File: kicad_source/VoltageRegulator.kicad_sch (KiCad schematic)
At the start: 40 parts, among them J10 x, J11 PowerPole, J12 Conn_01x02, Q2 IPD90P03P4L- 04, U12 INA226, U13 IFX91041EFJ

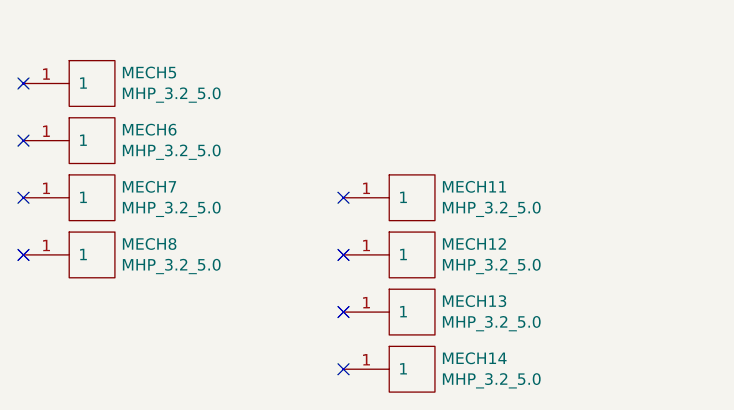
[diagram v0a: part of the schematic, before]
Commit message: added connector for quad encoder
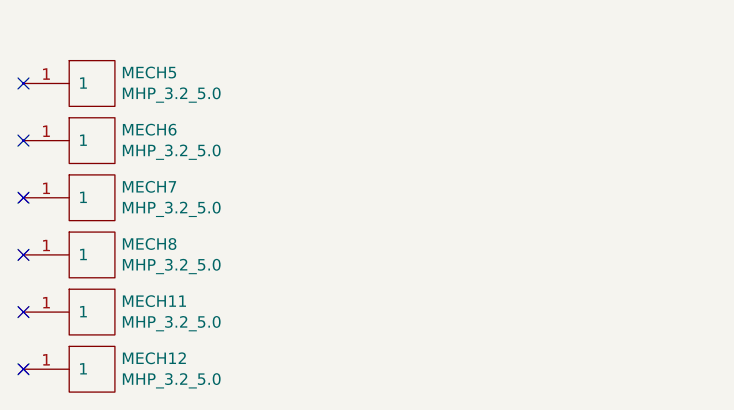
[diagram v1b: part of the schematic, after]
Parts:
- removed MECH13, MECH14: MHP_3.2_5.0, generationmake:MHP_3.2_5.8, symbol OpenCyphalRobotController07-rescue:MHP_3.2_5.0-MECH_mounting-holes
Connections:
- no-connect marks 9 -> 7
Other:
- moved on the sheet: MECH11, MECH12
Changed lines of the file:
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@@
   (junction (at 124.46 43.18) (diameter 0) (color 0 0 0 0)
   )
-  (no_connect (at 58.42 185.42))
   (no_connect (at 22.86 166.37))
   (no_connect (at 22.86 160.02))
   (no_connect (at 68.58 64.77))
   (no_connect (at 22.86 179.07))
-  (no_connect (at 58.42 172.72))
-  (no_connect (at 58.42 191.77))
-  (no_connect (at 58.42 179.07))
+  (no_connect (at 22.86 185.42))
+  (no_connect (at 22.86 191.77))
   (no_connect (at 22.86 172.72))
   (wire (pts (xy 189.23 128.27) (xy 189.23 127))
@@
     (pin "1")
   )
-  (symbol (lib_id "OpenCyphalRobotController07-rescue:MHP_3.2_5.0-MECH_mounting-holes") (at 66.04 172.72 0) (unit 1)
-    (in_bom yes) (on_board yes)
-    (property "Reference" "MECH11" (id 0) (at 69.2912 171.5516 0)
-      (effects (font (size 1.27 1.27)) (justify left))
-    )
-    (property "Value" "MHP_3.2_5.0" (id 1) (at 69.2912 173.863 0)
-      (effects (font (size 1.27 1.27)) (justify left))
-    )
-    (property "Footprint" "generationmake:MHP_3.2_5.8" (id 2) (at 63.5 171.45 0)
-      (effects (font (size 1.27 1.27)) hide)
-    )
-    (property "Datasheet" "" (id 3) (at 66.04 172.72 0)
-      (effects (font (size 1.27 1.27)) hide)
-    )
-    (pin "1")
-  )
-  (symbol (lib_id "OpenCyphalRobotController07-rescue:MHP_3.2_5.0-MECH_mounting-holes") (at 66.04 179.07 0) (unit 1)
-    (in_bom yes) (on_board yes)
-    (property "Reference" "MECH12" (id 0) (at 69.2912 177.9016 0)
-      (effects (font (size 1.27 1.27)) (justify left))
-    )
-    (property "Value" "MHP_3.2_5.0" (id 1) (at 69.2912 180.213 0)
-      (effects (font (size 1.27 1.27)) (justify left))
-    )
-    (property "Footprint" "generationmake:MHP_3.2_5.8" (id 2) (at 63.5 177.8 0)
-      (effects (font (size 1.27 1.27)) hide)
-    )
-    (property "Datasheet" "" (id 3) (at 66.04 179.07 0)
-      (effects (font (size 1.27 1.27)) hide)
-    )
-    (pin "1")
-  )
-  (symbol (lib_id "OpenCyphalRobotController07-rescue:MHP_3.2_5.0-MECH_mounting-holes") (at 66.04 185.42 0) (unit 1)
-    (in_bom yes) (on_board yes)
-    (property "Reference" "MECH13" (id 0) (at 69.2912 184.2516 0)
-      (effects (font (size 1.27 1.27)) (justify left))
-    )
-    (property "Value" "MHP_3.2_5.0" (id 1) (at 69.2912 186.563 0)
-      (effects (font (size 1.27 1.27)) (justify left))
-    )
-    (property "Footprint" "generationmake:MHP_3.2_5.8" (id 2) (at 63.5 184.15 0)
-      (effects (font (size 1.27 1.27)) hide)
-    )
-    (property "Datasheet" "" (id 3) (at 66.04 185.42 0)
-      (effects (font (size 1.27 1.27)) hide)
-    )
-    (pin "1")
-  )
-  (symbol (lib_id "OpenCyphalRobotController07-rescue:MHP_3.2_5.0-MECH_mounting-holes") (at 66.04 191.77 0) (unit 1)
-    (in_bom yes) (on_board yes)
-    (property "Reference" "MECH14" (id 0) (at 69.2912 190.6016 0)
-      (effects (font (size 1.27 1.27)) (justify left))
-    )
-    (property "Value" "MHP_3.2_5.0" (id 1) (at 69.2912 192.913 0)
-      (effects (font (size 1.27 1.27)) (justify left))
-    )
-    (property "Footprint" "generationmake:MHP_3.2_5.8" (id 2) (at 63.5 190.5 0)
-      (effects (font (size 1.27 1.27)) hide)
-    )
-    (property "Datasheet" "" (id 3) (at 66.04 191.77 0)
-      (effects (font (size 1.27 1.27)) hide)
-    )
+  (symbol (lib_id "OpenCyphalRobotController07-rescue:MHP_3.2_5.0-MECH_mounting-holes") (at 30.48 185.42 0) (unit 1)
+    (in_bom yes) (on_board yes)
+    (property "Reference" "MECH11" (id 0) (at 33.7312 184.2516 0)
+      (effects (font (size 1.27 1.27)) (justify left))
+    )
+    (property "Value" "MHP_3.2_5.0" (id 1) (at 33.7312 186.563 0)
+      (effects (font (size 1.27 1.27)) (justify left))
+    )
+    (property "Footprint" "generationmake:MHP_3.2_5.8" (id 2) (at 27.94 184.15 0)
+      (effects (font (size 1.27 1.27)) hide)
+    )
+    (property "Datasheet" "" (id 3) (at 30.48 185.42 0)
+      (effects (font (size 1.27 1.27)) hide)
+    )
+    (pin "1")
+  )
+  (symbol (lib_id "OpenCyphalRobotController07-rescue:MHP_3.2_5.0-MECH_mounting-holes") (at 30.48 191.77 0) (unit 1)
+    (in_bom yes) (on_board yes)
+    (property "Reference" "MECH12" (id 0) (at 33.7312 190.6016 0)
+      (effects (font (size 1.27 1.27)) (justify left))
+    )
+    (property "Value" "MHP_3.2_5.0" (id 1) (at 33.7312 192.913 0)
+      (effects (font (size 1.27 1.27)) (justify left))
+    )
+    (property "Footprint" "generationmake:MHP_3.2_5.8" (id 2) (at 27.94 190.5 0)
+      (effects (font (size 1.27 1.27)) hide)
+    )
+    (property "Datasheet" "" (id 3) (at 30.48 191.77 0)
+      (effects (font (size 1.27 1.27)) hide)
+    )

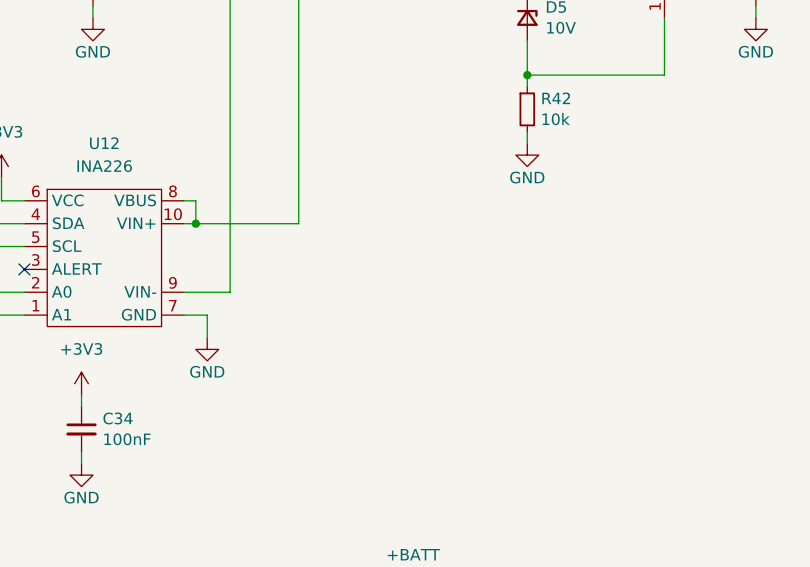
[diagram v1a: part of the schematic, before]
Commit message: updated schematic pdf
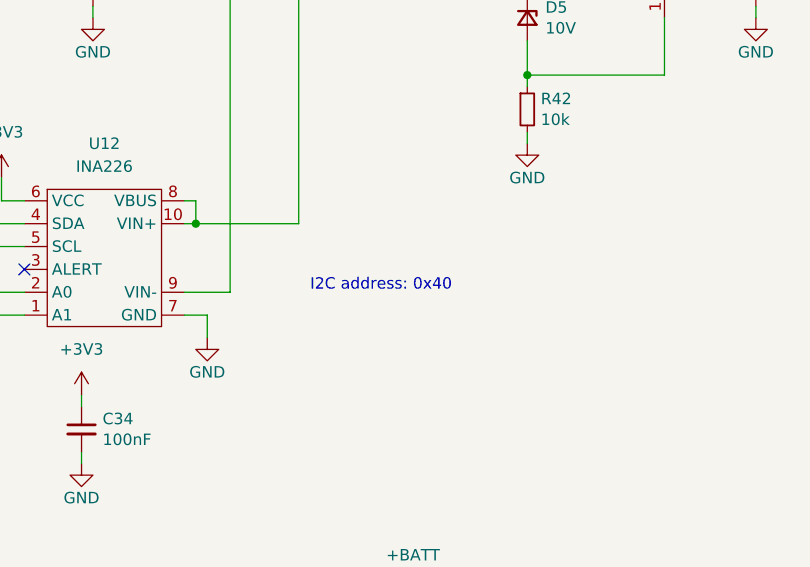
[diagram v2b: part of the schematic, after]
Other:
- note added: "I2C address: 0x40"
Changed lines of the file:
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@@
   (title_block
     (title "CyphalRobotController07/CAN")
-    (date "2023-10-01")
+    (date "2023-10-02")
     (rev "0.1")
     (company "generationmake")
@@
     (effects (font (size 1.524 1.524)) (justify left bottom))
   )
+  (text "I2C address: 0x40" (at 100.33 67.31 0)
+    (effects (font (size 1.27 1.27)) (justify left bottom))
+  )
   (text "measure up to +- 8.192 A" (at 78.74 19.05 0)

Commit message: updated 3d model to fit to reality
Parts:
- F2: footprint Fuse:Fuseholder_Blade_ATO_Littelfuse_Pudenz_2_Pin -> generationmake:Fuseholder_Blade_ATO_Littelfuse_Pudenz_2_Pin
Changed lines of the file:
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@@
   (title_block
     (title "CyphalRobotController07/CAN")
-    (date "2023-10-02")
+    (date "2023-11-15")
     (rev "0.1")
     (company "generationmake")
@@
     (property "Reference" "F2" (id 0) (at 165.1 24.13 0))
     (property "Value" "Fuse_Small" (id 1) (at 165.1 26.67 0))
-    (property "Footprint" "Fuse:Fuseholder_Blade_ATO_Littelfuse_Pudenz_2_Pin" (id 2) (at 165.1 29.21 0)
-      (effects (font (size 1.27 1.27)) hide)
-    )
+    (property "Footprint" "generationmake:Fuseholder_Blade_ATO_Littelfuse_Pudenz_2_Pin" (id 2) (at 165.1 29.21 0)
+      (effects (font (size 1.27 1.27)) hide)
+    )

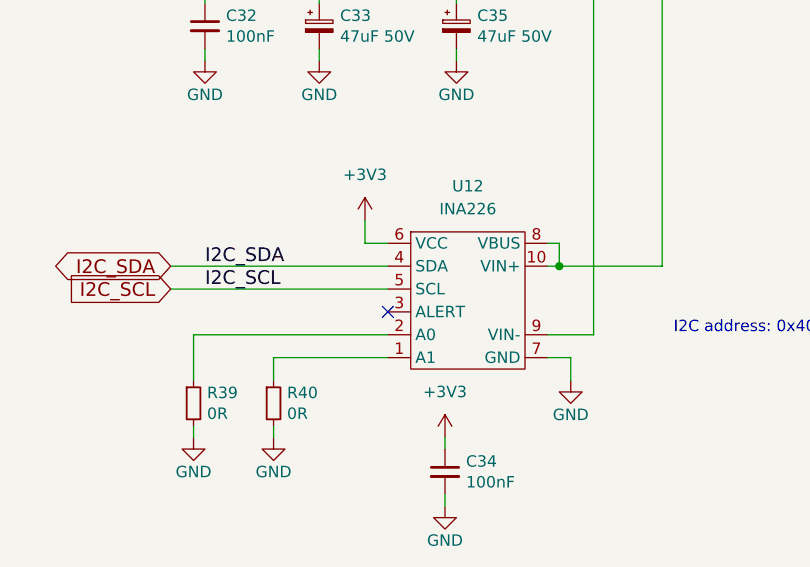
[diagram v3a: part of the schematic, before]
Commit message: combined 3.3V nets
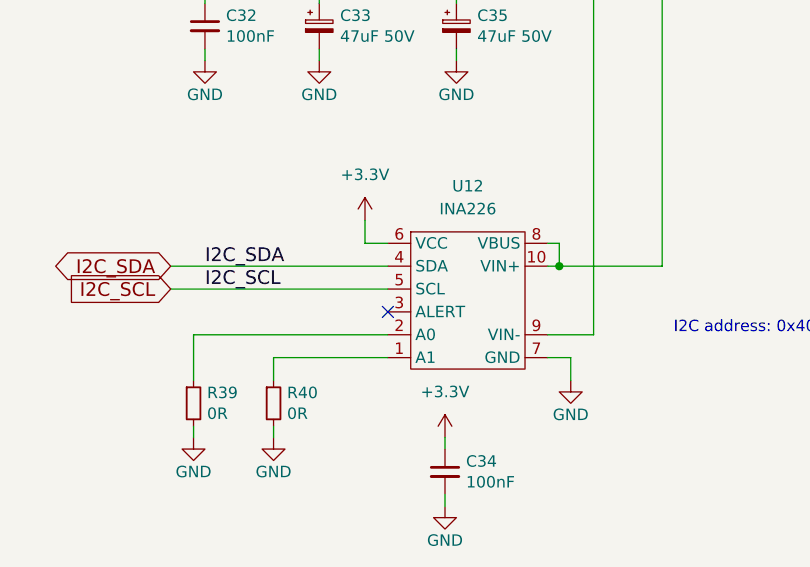
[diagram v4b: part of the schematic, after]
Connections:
- net +3V3 renamed +3.3V
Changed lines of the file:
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@@
   (title_block
     (title "CyphalRobotController07/CAN")
-    (date "2023-11-15")
-    (rev "0.1")
+    (date "2023-12-03")
+    (rev "0.2")
     (company "generationmake")
   )
@@
     (pin "2")
   )
+  (symbol (lib_id "power:+3.3V") (at 66.04 54.61 0) (unit 1)
+    (in_bom yes) (on_board yes) (fields_autoplaced)
+    (property "Reference" "#PWR0153" (id 0) (at 66.04 58.42 0)
+      (effects (font (size 1.27 1.27)) hide)
+    )
+    (property "Value" "+3.3V" (id 1) (at 66.04 49.53 0))
+    (property "Footprint" "" (id 2) (at 66.04 54.61 0)
+      (effects (font (size 1.27 1.27)) hide)
+    )
+    (property "Datasheet" "" (id 3) (at 66.04 54.61 0)
+      (effects (font (size 1.27 1.27)) hide)
+    )
+    (pin "1")
+  )
   (symbol (lib_id "power:GND") (at 149.86 36.83 0) (unit 1)
     (in_bom yes) (on_board yes)
@@
     (pin "2")
   )
-  (symbol (lib_id "power:+3V3") (at 74.93 78.74 0) (unit 1)
-    (in_bom yes) (on_board yes) (fields_autoplaced)
-    (property "Reference" "#PWR0101" (id 0) (at 74.93 82.55 0)
-      (effects (font (size 1.27 1.27)) hide)
-    )
-    (property "Value" "+3V3" (id 1) (at 74.93 73.66 0))
-    (property "Footprint" "" (id 2) (at 74.93 78.74 0)
-      (effects (font (size 1.27 1.27)) hide)
-    )
-    (property "Datasheet" "" (id 3) (at 74.93 78.74 0)
-      (effects (font (size 1.27 1.27)) hide)
-    )
-    (pin "1")
-  )
   (symbol (lib_id "power:+BATT") (at 111.76 101.6 0) (unit 1)
     (in_bom yes) (on_board yes) (fields_autoplaced)
@@
     (pin "1")
   )
+  (symbol (lib_id "power:+3.3V") (at 74.93 78.74 0) (unit 1)
+    (in_bom yes) (on_board yes) (fields_autoplaced)
+    (property "Reference" "#PWR0152" (id 0) (at 74.93 82.55 0)
+      (effects (font (size 1.27 1.27)) hide)
+    )
+    (property "Value" "+3.3V" (id 1) (at 74.93 73.66 0))
+    (property "Footprint" "" (id 2) (at 74.93 78.74 0)
+      (effects (font (size 1.27 1.27)) hide)
+    )
+    (property "Datasheet" "" (id 3) (at 74.93 78.74 0)
+      (effects (font (size 1.27 1.27)) hide)
+    )
+    (pin "1")
+  )
   (symbol (lib_id "power:GND") (at 60.96 36.83 0) (unit 1)
     (in_bom yes) (on_board yes)
@@
     (pin "2")
   )
-  (symbol (lib_id "power:+3V3") (at 66.04 54.61 0) (unit 1)
-    (in_bom yes) (on_board yes) (fields_autoplaced)
-    (property "Reference" "#PWR0100" (id 0) (at 66.04 58.42 0)
-      (effects (font (size 1.27 1.27)) hide)
-    )
-    (property "Value" "+3V3" (id 1) (at 66.04 49.53 0))
-    (property "Footprint" "" (id 2) (at 66.04 54.61 0)
-      (effects (font (size 1.27 1.27)) hide)
-    )
-    (property "Datasheet" "" (id 3) (at 66.04 54.61 0)
-      (effects (font (size 1.27 1.27)) hide)
-    )
-    (pin "1")
-  )
   (symbol (lib_id "Device:R_Small") (at 95.25 29.21 90) (unit 1)

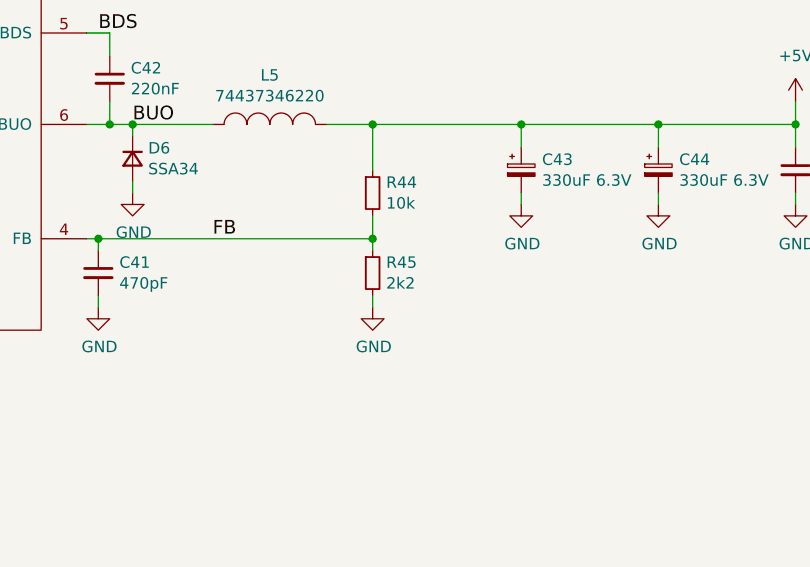
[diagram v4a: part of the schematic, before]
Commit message: changed R45 to 1k3
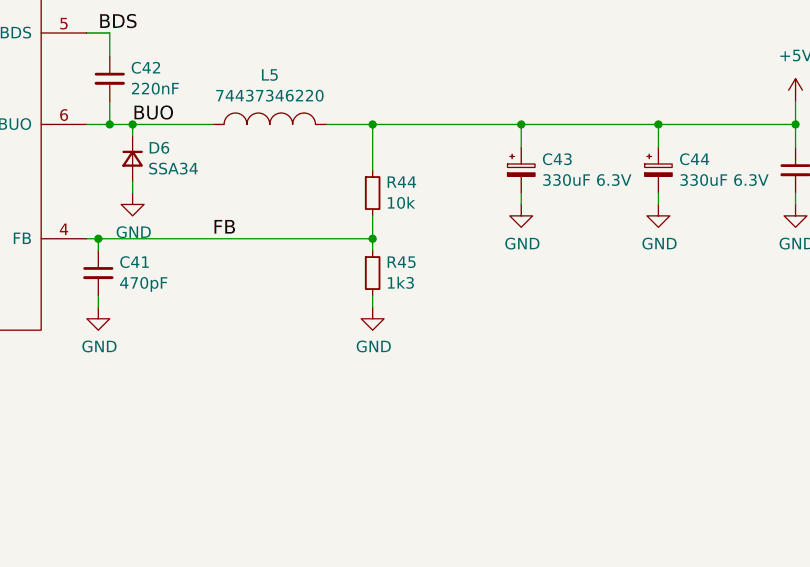
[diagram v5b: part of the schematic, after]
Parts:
- R45: value 2k2 -> 1k3
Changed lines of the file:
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@@
       (effects (font (size 1.27 1.27)) (justify left))
     )
-    (property "Value" "2k2" (id 1) (at 217.3986 138.303 0)
+    (property "Value" "1k3" (id 1) (at 217.3986 138.303 0)
       (effects (font (size 1.27 1.27)) (justify left))
     )

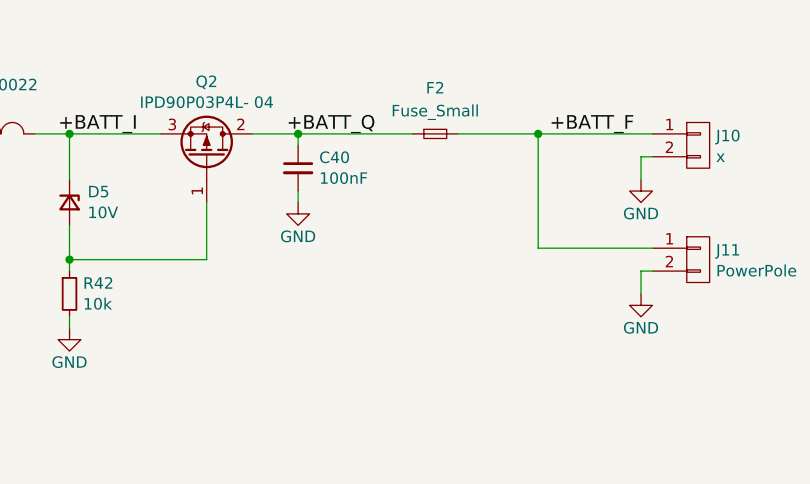
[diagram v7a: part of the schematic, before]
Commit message: added tvs diode on input
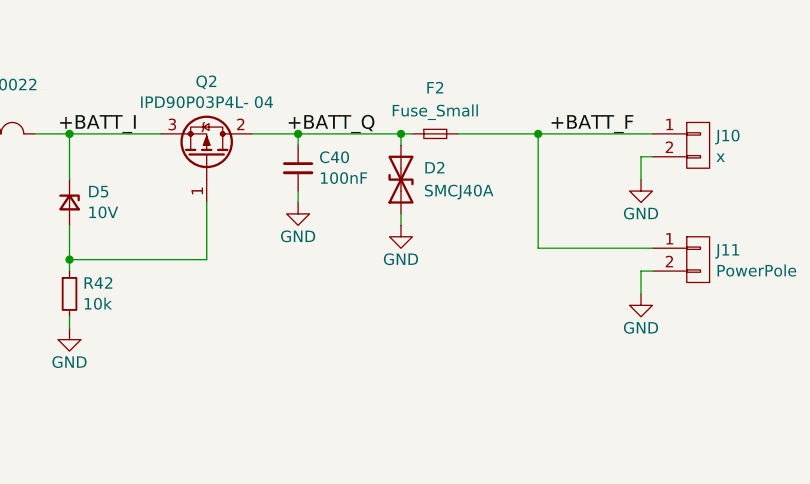
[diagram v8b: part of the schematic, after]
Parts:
- added D2: SMCJ40A, Diode_SMD:D_SMC, symbol Device:D_TVS
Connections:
- net +BATT_Q: now also D2.2 (A2)
- net GND: now also D2.1 (A1)
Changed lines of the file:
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@@
   (junction (at 87.63 59.69) (diameter 0) (color 0 0 0 0)
+  )
+  (junction (at 161.29 29.21) (diameter 0) (color 0 0 0 0)
   )
   (junction (at 186.69 120.65) (diameter 0) (color 0 0 0 0)
@@
     (stroke (width 0) (type default) (color 0 0 0 0))
   )
-  (wire (pts (xy 149.86 29.21) (xy 162.56 29.21))
+  (wire (pts (xy 149.86 29.21) (xy 161.29 29.21))
     (stroke (width 0) (type default) (color 0 0 0 0))
   )
@@
     (stroke (width 0) (type default) (color 0 0 0 0))
   )
+  (wire (pts (xy 161.29 38.1) (xy 161.29 39.37))
+    (stroke (width 0) (type default) (color 0 0 0 0))
+  )
   (wire (pts (xy 146.05 127) (xy 143.51 127))
     (stroke (width 0) (type default) (color 0 0 0 0))
   )
+  (wire (pts (xy 161.29 29.21) (xy 161.29 30.48))
+    (stroke (width 0) (type default) (color 0 0 0 0))
+  )
   (wire (pts (xy 111.76 104.14) (xy 115.57 104.14))
     (stroke (width 0) (type default) (color 0 0 0 0))
@@
   )
   (wire (pts (xy 176.53 29.21) (xy 176.53 41.91))
+    (stroke (width 0) (type default) (color 0 0 0 0))
+  )
+  (wire (pts (xy 161.29 29.21) (xy 162.56 29.21))
     (stroke (width 0) (type default) (color 0 0 0 0))
   )
@@
     (pin "2")
   )
+  (symbol (lib_id "power:GND") (at 161.29 39.37 0) (unit 1)
+    (in_bom yes) (on_board yes)
+    (property "Reference" "#PWR021" (id 0) (at 161.29 45.72 0)
+      (effects (font (size 1.27 1.27)) hide)
+    )
+    (property "Value" "GND" (id 1) (at 161.29 43.18 0))
+    (property "Footprint" "" (id 2) (at 161.29 39.37 0))
+    (property "Datasheet" "" (id 3) (at 161.29 39.37 0))
+    (pin "1")
+  )
   (symbol (lib_id "power:+BATT") (at 111.76 101.6 0) (unit 1)
     (in_bom yes) (on_board yes) (fields_autoplaced)
@@
     (pin "1")
   )
+  (symbol (lib_id "Device:D_TVS") (at 161.29 34.29 90) (unit 1)
+    (in_bom yes) (on_board yes) (fields_autoplaced)
+    (property "Reference" "D2" (id 0) (at 163.83 33.0199 90)
+      (effects (font (size 1.27 1.27)) (justify right))
+    )
+    (property "Value" "SMCJ40A" (id 1) (at 163.83 35.5599 90)
+      (effects (font (size 1.27 1.27)) (justify right))
+    )
+    (property "Footprint" "Diode_SMD:D_SMC" (id 2) (at 161.29 34.29 0)
+      (effects (font (size 1.27 1.27)) hide)
+    )
+    (property "Datasheet" "~" (id 3) (at 161.29 34.29 0)
+      (effects (font (size 1.27 1.27)) hide)
+    )
+    (pin "1")
+    (pin "2")
+  )
   (symbol (lib_id "power:GND") (at 60.96 36.83 0) (unit 1)
